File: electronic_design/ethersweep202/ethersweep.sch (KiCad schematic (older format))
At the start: 88 parts, among them J1 AVR-ISP-6, J10 HR911105A, J2 Conn_01x02_Male, J3 Conn_01x04_Female, J4 Conn_01x02_Male, J5 Conn_01x02_Male, J6 Conn_01x07_Female, J7 Conn_01x07_Male, J8 AVR-ISP-6, M1 Stepper_Motor_bipolar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

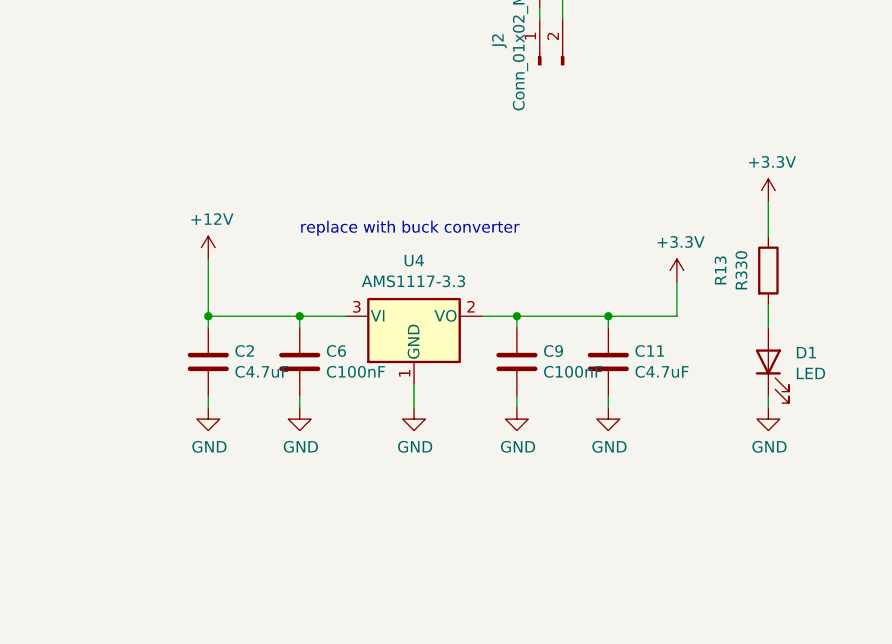
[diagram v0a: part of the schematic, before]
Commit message: major power supply canges
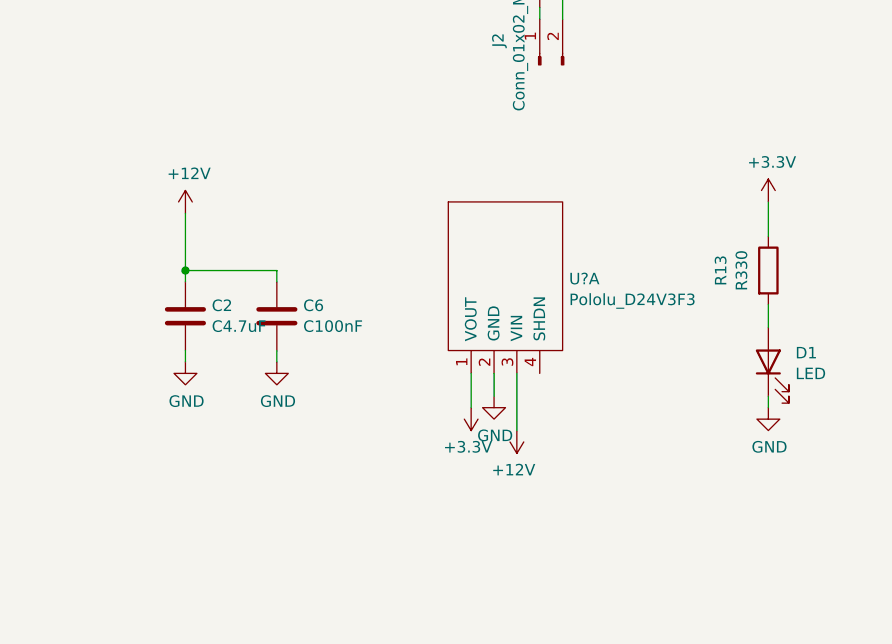
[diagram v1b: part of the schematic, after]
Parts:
- removed C11: C4.7uF, Capacitor_SMD:C_1206_3216Metric, symbol Device:C
- removed C9: C100nF, Capacitor_SMD:C_0805_2012Metric, symbol Device:C
- removed U4: AMS1117-3.3, Package_TO_SOT_SMD:SOT-223-3_TabPin2, symbol Regulator_Linear:AMS1117-3.3
- added U?: Pololu_D24V3F3, symbol power:Pololu_D24V3F3
- J2: footprint Connector_AMASS:AMASS_XT60-M_1x02_P7.20mm_Vertical -> Connector_AMASS:AMASS_XT30PW-M_1x02_P2.50mm_Horizontal
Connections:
- net +12V: now also U?.3 (VIN)
- net +3V3: now also U?.1 (VOUT)
- net GND: now also U?.2 (GND)
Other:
- note removed: "replace with buck converter"
- moved on the sheet: C2, C6
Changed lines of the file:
@@
 	1    0    0    -1
 $EndComp
-$Comp
-L Device:C C9
-U 1 1 608443F6
-P 13800 2700
-F 0 "C9" H 13915 2746 50  0000 L CNN
-F 1 "C100nF" H 13915 2655 50  0000 L CNN
-F 2 "Capacitor_SMD:C_0805_2012Metric" H 13838 2550 50  0001 C CNN
-F 3 "~" H 13800 2700 50  0001 C CNN
-F 4 "C49678" H 13800 2700 50  0001 C CNN "LCSC"
-	1    13800 2700
-	1    0    0    -1
-$EndComp
-$Comp
-L power:GND #PWR0128
-U 1 1 60860F83
-P 14200 2900
-F 0 "#PWR0128" H 14200 2650 50  0001 C CNN
-F 1 "GND" H 14205 2727 50  0000 C CNN
-F 2 "" H 14200 2900 50  0001 C CNN
-F 3 "" H 14200 2900 50  0001 C CNN
-	1    14200 2900
-	1    0    0    -1
-$EndComp
-Wire Wire Line
-	14200 2850 14200 2900
-$Comp
-L power:GND #PWR0129
-U 1 1 60860F8A
-P 13800 2900
-F 0 "#PWR0129" H 13800 2650 50  0001 C CNN
-F 1 "GND" H 13805 2727 50  0000 C CNN
-F 2 "" H 13800 2900 50  0001 C CNN
-F 3 "" H 13800 2900 50  0001 C CNN
-	1    13800 2900
-	1    0    0    -1
-$EndComp
-Wire Wire Line
-	13800 2850 13800 2900
-Wire Wire Line
-	13650 2500 13800 2500
-Wire Wire Line
-	13800 2500 13800 2550
-Wire Wire Line
-	13800 2500 14200 2500
-Wire Wire Line
-	14200 2500 14200 2550
-Connection ~ 13800 2500
-Wire Wire Line
-	14200 2500 14500 2500
-Wire Wire Line
-	14500 2500 14500 2350
-Connection ~ 14200 2500
-Wire Wire Line
-	13350 2800 13350 2900
-Connection ~ 12850 2500
-Wire Wire Line
-	12850 2500 13050 2500
-Wire Wire Line
-	12850 2500 12850 2550
-Wire Wire Line
-	12450 2500 12850 2500
-Wire Wire Line
-	12450 2500 12450 2550
-$Comp
-L power:+3.3V #PWR0130
-U 1 1 608670E7
-P 14500 2350
-F 0 "#PWR0130" H 14500 2200 50  0001 C CNN
-F 1 "+3.3V" H 14515 2523 50  0000 C CNN
-F 2 "" H 14500 2350 50  0001 C CNN
-F 3 "" H 14500 2350 50  0001 C CNN
-	1    14500 2350
-	1    0    0    -1
-$EndComp
-Wire Wire Line
-	12450 2850 12450 2900
+Wire Wire Line
+	12750 2300 12750 2350
+Wire Wire Line
+	12350 2300 12750 2300
+Wire Wire Line
+	12350 2300 12350 2350
+Wire Wire Line
+	12350 2650 12350 2700
 $Comp
 L power:GND #PWR0127
 U 1 1 6085E20F
-P 12450 2900
-F 0 "#PWR0127" H 12450 2650 50  0001 C CNN
-F 1 "GND" H 12455 2727 50  0000 C CNN
-F 2 "" H 12450 2900 50  0001 C CNN
-F 3 "" H 12450 2900 50  0001 C CNN
-	1    12450 2900
-	1    0    0    -1
-$EndComp
-Wire Wire Line
-	12850 2850 12850 2900
+P 12350 2700
+F 0 "#PWR0127" H 12350 2450 50  0001 C CNN
+F 1 "GND" H 12355 2527 50  0000 C CNN
+F 2 "" H 12350 2700 50  0001 C CNN
+F 3 "" H 12350 2700 50  0001 C CNN
+	1    12350 2700
+	1    0    0    -1
+$EndComp
+Wire Wire Line
+	12750 2650 12750 2700
 $Comp
 L power:GND #PWR0126
 U 1 1 6085B87D
-P 12850 2900
-F 0 "#PWR0126" H 12850 2650 50  0001 C CNN
-F 1 "GND" H 12855 2727 50  0000 C CNN
-F 2 "" H 12850 2900 50  0001 C CNN
-F 3 "" H 12850 2900 50  0001 C CNN
-	1    12850 2900
+P 12750 2700
+F 0 "#PWR0126" H 12750 2450 50  0001 C CNN
+F 1 "GND" H 12755 2527 50  0000 C CNN
+F 2 "" H 12750 2700 50  0001 C CNN
+F 3 "" H 12750 2700 50  0001 C CNN
+	1    12750 2700
 	1    0    0    -1
 $EndComp
@@
 L Device:C C6
 U 1 1 6083E077
-P 12850 2700
-F 0 "C6" H 12965 2746 50  0000 L CNN
-F 1 "C100nF" H 12965 2655 50  0000 L CNN
-F 2 "Capacitor_SMD:C_0805_2012Metric" H 12888 2550 50  0001 C CNN
-F 3 "~" H 12850 2700 50  0001 C CNN
-F 4 "C49678" H 12850 2700 50  0001 C CNN "LCSC"
-	1    12850 2700
-	1    0    0    -1
-$EndComp
-$Comp
-L power:GND #PWR0122
-U 1 1 6082DD86
-P 13350 2900
-F 0 "#PWR0122" H 13350 2650 50  0001 C CNN
-F 1 "GND" H 13355 2727 50  0000 C CNN
-F 2 "" H 13350 2900 50  0001 C CNN
-F 3 "" H 13350 2900 50  0001 C CNN
-	1    13350 2900
-	1    0    0    -1
-$EndComp
-$Comp
-L Regulator_Linear:AMS1117-3.3 U4
-U 1 1 6082A4D2
-P 13350 2500
-F 0 "U4" H 13350 2742 50  0000 C CNN
-F 1 "AMS1117-3.3" H 13350 2651 50  0000 C CNN
-F 2 "Package_TO_SOT_SMD:SOT-223-3_TabPin2" H 13350 2700 50  0001 C CNN
-F 3 "http://www.advanced-monolithic.com/pdf/ds1117.pdf" H 13450 2250 50  0001 C CNN
-F 4 "C6186" H 13350 2500 50  0001 C CNN "LCSC"
-	1    13350 2500
+P 12750 2500
+F 0 "C6" H 12865 2546 50  0000 L CNN
+F 1 "C100nF" H 12865 2455 50  0000 L CNN
+F 2 "Capacitor_SMD:C_0805_2012Metric" H 12788 2350 50  0001 C CNN
+F 3 "~" H 12750 2500 50  0001 C CNN
+F 4 "C49678" H 12750 2500 50  0001 C CNN "LCSC"
+	1    12750 2500
 	1    0    0    -1
 $EndComp
@@
 MOSI
 Wire Wire Line
-	12450 2500 12450 2250
+	12350 2300 12350 2050
 $Comp
 L power:+12V #PWR0101
 U 1 1 6057C188
-P 12450 2250
-F 0 "#PWR0101" H 12450 2100 50  0001 C CNN
-F 1 "+12V" H 12465 2423 50  0000 C CNN
-F 2 "" H 12450 2250 50  0001 C CNN
-F 3 "" H 12450 2250 50  0001 C CNN
-	1    12450 2250
-	1    0    0    -1
-$EndComp
-Connection ~ 12450 2500
+P 12350 2050
+F 0 "#PWR0101" H 12350 1900 50  0001 C CNN
+F 1 "+12V" H 12365 2223 50  0000 C CNN
+F 2 "" H 12350 2050 50  0001 C CNN
+F 3 "" H 12350 2050 50  0001 C CNN
+	1    12350 2050
+	1    0    0    -1
+$EndComp
+Connection ~ 12350 2300
 Wire Wire Line
 	4450 3500 4350 3500
@@
 L Device:C C2
 U 1 1 6038787C
-P 12450 2700
-F 0 "C2" H 12565 2746 50  0000 L CNN
-F 1 "C4.7uF" H 12565 2655 50  0000 L CNN
-F 2 "Capacitor_SMD:C_1206_3216Metric" H 12488 2550 50  0001 C CNN
-F 3 "~" H 12450 2700 50  0001 C CNN
-F 4 "C29823" H 12450 2700 50  0001 C CNN "LCSC"
-	1    12450 2700
-	1    0    0    -1
-$EndComp
-$Comp
-L Device:C C11
-U 1 1 6039E0FF
-P 14200 2700
-F 0 "C11" H 14315 2746 50  0000 L CNN
-F 1 "C4.7uF" H 14315 2655 50  0000 L CNN
-F 2 "Capacitor_SMD:C_1206_3216Metric" H 14238 2550 50  0001 C CNN
-F 3 "~" H 14200 2700 50  0001 C CNN
-F 4 "C29823" H 14200 2700 50  0001 C CNN "LCSC"
-	1    14200 2700
+P 12350 2500
+F 0 "C2" H 12465 2546 50  0000 L CNN
+F 1 "C4.7uF" H 12465 2455 50  0000 L CNN
+F 2 "Capacitor_SMD:C_1206_3216Metric" H 12388 2350 50  0001 C CNN
+F 3 "~" H 12350 2500 50  0001 C CNN
+F 4 "C29823" H 12350 2500 50  0001 C CNN "LCSC"
+	1    12350 2500
 	1    0    0    -1
 $EndComp
@@
 F 0 "J2" H 14008 1581 50  0000 C CNN
 F 1 "Conn_01x02_Male" H 14008 1490 50  0000 C CNN
-F 2 "Connector_AMASS:AMASS_XT60-M_1x02_P7.20mm_Vertical" H 13900 1400 50  0001 C CNN
+F 2 "Connector_AMASS:AMASS_XT30PW-M_1x02_P2.50mm_Horizontal" H 13900 1400 50  0001 C CNN
 F 3 "~" H 13900 1400 50  0001 C CNN
 	1    13900 1400
@@
 	0    -1   -1   0
 $EndComp
-Text Notes 12850 2150 0    50   ~ 0
-replace with buck converter
 $Comp
 L power:+3.3VA #PWR0204
@@
 	1    0    0    -1
 $EndComp
+$Comp
+L power:Pololu_D24V3F3 U?
+U 1 1 606667BB
+P 13750 1950
+F 0 "U?" H 14028 1563 50  0000 L CNN
+F 1 "Pololu_D24V3F3" H 14028 1472 50  0000 L CNN
+F 2 "" H 13700 2050 50  0001 C CNN
+F 3 "" H 13700 2050 50  0001 C CNN
+	1    13750 1950
+	1    0    0    -1
+$EndComp
+Wire Wire Line
+	13700 2750 13700 2850
+$Comp
+L power:GND #PWR?
+U 1 1 60667739
+P 13700 2850
+F 0 "#PWR?" H 13700 2600 50  0001 C CNN
+F 1 "GND" H 13705 2677 50  0000 C CNN
+F 2 "" H 13700 2850 50  0001 C CNN
+F 3 "" H 13700 2850 50  0001 C CNN
+	1    13700 2850
+	1    0    0    -1
+$EndComp
+Wire Wire Line
+	13600 2750 13600 2900
+$Comp
+L power:+3.3V #PWR?
+U 1 1 606ABE68
+P 13600 2900
+F 0 "#PWR?" H 13600 2750 50  0001 C CNN
+F 1 "+3.3V" H 13615 3073 50  0000 C CNN
+F 2 "" H 13600 2900 50  0001 C CNN
+F 3 "" H 13600 2900 50  0001 C CNN
+	1    13600 2900
+	-1   0    0    1
+$EndComp
+Wire Wire Line
+	13800 2750 13800 3000
+$Comp
+L power:+12V #PWR?
+U 1 1 606CDB4B
+P 13800 3000
+F 0 "#PWR?" H 13800 2850 50  0001 C CNN
+F 1 "+12V" H 13815 3173 50  0000 C CNN
+F 2 "" H 13800 3000 50  0001 C CNN
+F 3 "" H 13800 3000 50  0001 C CNN
+	1    13800 3000
+	-1   0    0    1
+$EndComp
 $EndSCHEMATC

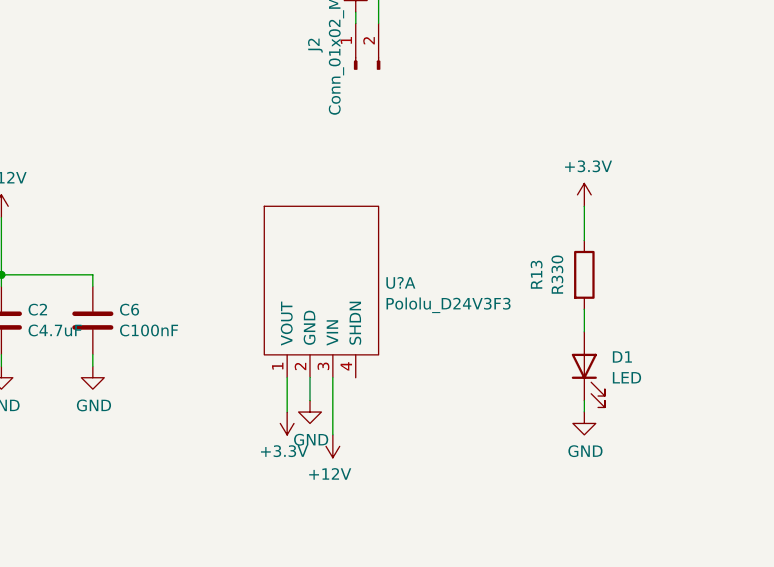
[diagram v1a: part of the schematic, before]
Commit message: layout changes, added status led ...
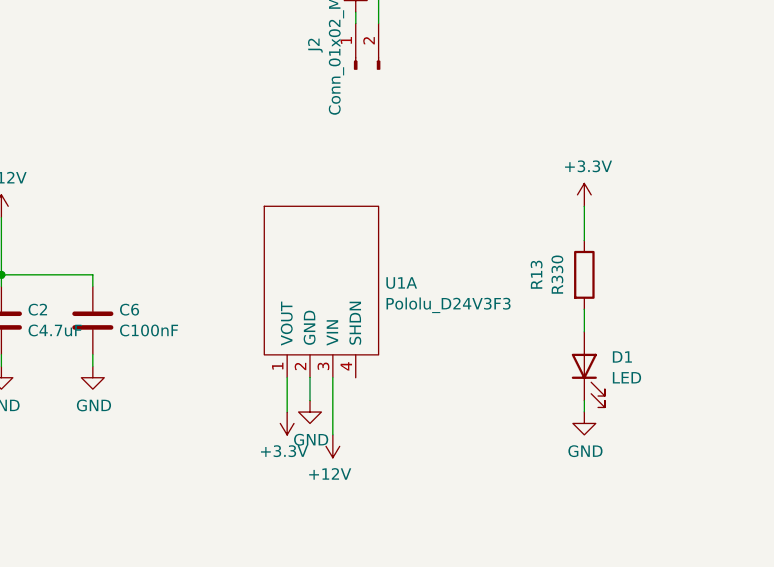
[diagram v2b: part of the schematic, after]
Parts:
- U1: renamed from U?; footprint (none) -> Module:Pololu_D24V3F3
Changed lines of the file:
@@
 $EndComp
 $Comp
-L power:Pololu_D24V3F3 U?
+L power:Pololu_D24V3F3 U1
 U 1 1 606667BB
 P 13750 1950
-F 0 "U?" H 14028 1563 50  0000 L CNN
+F 0 "U1" H 14028 1563 50  0000 L CNN
 F 1 "Pololu_D24V3F3" H 14028 1472 50  0000 L CNN
-F 2 "" H 13700 2050 50  0001 C CNN
+F 2 "Module:Pololu_D24V3F3" H 13700 2050 50  0001 C CNN
 F 3 "" H 13700 2050 50  0001 C CNN
 	1    13750 1950
@@
 	13700 2750 13700 2850
 $Comp
-L power:GND #PWR?
+L power:GND #PWR0122
 U 1 1 60667739
 P 13700 2850
-F 0 "#PWR?" H 13700 2600 50  0001 C CNN
+F 0 "#PWR0122" H 13700 2600 50  0001 C CNN
 F 1 "GND" H 13705 2677 50  0000 C CNN
 F 2 "" H 13700 2850 50  0001 C CNN
@@
 	13600 2750 13600 2900
 $Comp
-L power:+3.3V #PWR?
+L power:+3.3V #PWR0128
 U 1 1 606ABE68
 P 13600 2900
-F 0 "#PWR?" H 13600 2750 50  0001 C CNN
+F 0 "#PWR0128" H 13600 2750 50  0001 C CNN
 F 1 "+3.3V" H 13615 3073 50  0000 C CNN
 F 2 "" H 13600 2900 50  0001 C CNN
@@
 	13800 2750 13800 3000
 $Comp
-L power:+12V #PWR?
+L power:+12V #PWR0129
 U 1 1 606CDB4B
 P 13800 3000
-F 0 "#PWR?" H 13800 2850 50  0001 C CNN
+F 0 "#PWR0129" H 13800 2850 50  0001 C CNN
 F 1 "+12V" H 13815 3173 50  0000 C CNN
 F 2 "" H 13800 3000 50  0001 C CNN
